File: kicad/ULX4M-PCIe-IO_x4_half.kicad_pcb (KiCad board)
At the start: 4 copper layers, 167.7 x 111.2 mm, 30 parts, among them J1 PCIexpress_bracket, J2 PCIexpress_x4, J3 SFP+, J4 SFP+, J5 Conn_02x20_Odd_Even, J6 Conn_02x05_Odd_Even, J7 Micro_SD_Card_CD, J8 Conn_02x05_Odd_Even, P2 HDMI-D, SW1 SW_DIP_x08, SW2 SW_DIP_x08, U1 Raspberry_Pi_Compute_Module_4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

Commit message: Modules update
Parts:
- removed U1: Raspberry_Pi_Compute_Module_4_Compute_Module_4_Functional, cm4:Raspberry-Pi-4-Compute-Module
- added Module1: ComputeModule4-CM4, CM4IO:Raspberry-Pi-4-Compute-Module, F.Cu at (161.2, 119.8)
- added P1: HDMI-D, hdmi-d:HDMI-D, F.Cu at (117.5, 73.9)
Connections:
- AE1 pad 1: (no net) -> unconnected-(AE1-Pad1)
- AE1 pad 2: Net-(AE1-Pad2) -> unconnected-(AE1-Pad2)
- AE2 pad 1: (no net) -> unconnected-(AE2-Pad1)
- AE2 pad 2: Net-(AE2-Pad2) -> unconnected-(AE2-Pad2)
- C1 pad 1: (no net) -> /PER0_P
- C2 pad 2: (no net) -> /PER0_N
- C3 pad 1: (no net) -> /PER1_P
- C4 pad 2: (no net) -> /PER1_N
- C5 pad 1: (no net) -> /PER2_P
- C6 pad 2: (no net) -> /PER2_N
- C7 pad 1: (no net) -> /PER3_P
- C8 pad 2: (no net) -> /PER3_N
- J2 pad A1: (no net) -> /~{PRSNT1}
- J2 pad A11: (no net) -> /~{PERST}
- J2 pad A13: (no net) -> /REFCLK+
- J2 pad A14: (no net) -> /REFCLK-
- J2 pad A19: (no net) -> unconnected-(J2-RSVD)_1
- J2 pad A32: (no net) -> unconnected-(J2-RSVD)_2
- J2 pad A5: (no net) -> /TCK
- J2 pad A6: (no net) -> /TDI
- J2 pad A7: (no net) -> /TDO
- J2 pad A8: (no net) -> /TMS
- J2 pad B10: (no net) -> +3.3VA
- J2 pad B11: (no net) -> /~{WAKE}
- J2 pad B12: (no net) -> unconnected-(J2-RSVD)_3
- J2 pad B17: (no net) -> /~{PRSNT2x1}
- J2 pad B30: (no net) -> unconnected-(J2-RSVD)
- J2 pad B31: (no net) -> /~{PRSNT2x4}
- J2 pad B5: (no net) -> /SMCLK
- J2 pad B6: (no net) -> /SMDAT
- J2 pad B9: (no net) -> /~{TRST}
- J3 pad 12: (no net) -> unconnected-(J3-RD-)
- J3 pad 13: (no net) -> unconnected-(J3-RD+)
- J3 pad 15: (no net) -> unconnected-(J3-VccR)
- J3 pad 16: (no net) -> unconnected-(J3-VccT)
- J3 pad 18: (no net) -> unconnected-(J3-TD+)
- J3 pad 19: (no net) -> unconnected-(J3-TD-)
- J3 pad 2: (no net) -> unconnected-(J3-TX_FAULT)
- J3 pad 3: (no net) -> unconnected-(J3-TX_DISABLE)
- J3 pad 4: (no net) -> unconnected-(J3-SDA)
- J3 pad 5: (no net) -> unconnected-(J3-SCL)
- J3 pad 6: (no net) -> unconnected-(J3-MOD_ABS)
- J3 pad 7: (no net) -> unconnected-(J3-RS0)
- J3 pad 8: (no net) -> unconnected-(J3-RX_LOS)
- J3 pad 9: (no net) -> unconnected-(J3-RS1)
- J3 pad CAGE: Net-(J3-PadCAGE) -> unconnected-(J3-PadCAGE)
- J4 pad 12: (no net) -> unconnected-(J4-RD-)
- J4 pad 13: (no net) -> unconnected-(J4-RD+)
- J4 pad 15: (no net) -> unconnected-(J4-VccR)
- J4 pad 16: (no net) -> unconnected-(J4-VccT)
- J4 pad 18: (no net) -> unconnected-(J4-TD+)
- J4 pad 19: (no net) -> unconnected-(J4-TD-)
- J4 pad 2: (no net) -> unconnected-(J4-TX_FAULT)
- J4 pad 3: (no net) -> unconnected-(J4-TX_DISABLE)
- J4 pad 4: (no net) -> unconnected-(J4-SDA)
- J4 pad 5: (no net) -> unconnected-(J4-SCL)
- J4 pad 6: (no net) -> unconnected-(J4-MOD_ABS)
- J4 pad 7: (no net) -> unconnected-(J4-RS0)
- J4 pad 8: (no net) -> unconnected-(J4-RX_LOS)
- J4 pad 9: (no net) -> unconnected-(J4-RS1)
- J4 pad CAGE: Net-(J4-PadCAGE) -> unconnected-(J4-PadCAGE)
- J5 pad 1: (no net) -> unconnected-(J5-Pin_1)
- J5 pad 10: (no net) -> unconnected-(J5-Pin_10)
- J5 pad 11: (no net) -> unconnected-(J5-Pin_11)
- J5 pad 12: (no net) -> unconnected-(J5-Pin_12)
- J5 pad 13: (no net) -> unconnected-(J5-Pin_13)
- J5 pad 14: (no net) -> unconnected-(J5-Pin_14)
- J5 pad 15: (no net) -> unconnected-(J5-Pin_15)
- J5 pad 16: (no net) -> unconnected-(J5-Pin_16)
- J5 pad 17: (no net) -> unconnected-(J5-Pin_17)
- J5 pad 18: (no net) -> unconnected-(J5-Pin_18)
- J5 pad 19: (no net) -> unconnected-(J5-Pin_19)
- J5 pad 2: (no net) -> unconnected-(J5-Pin_2)
- J5 pad 20: (no net) -> unconnected-(J5-Pin_20)
- J5 pad 21: (no net) -> unconnected-(J5-Pin_21)
- J5 pad 22: (no net) -> unconnected-(J5-Pin_22)
- J5 pad 23: (no net) -> unconnected-(J5-Pin_23)
- J5 pad 24: (no net) -> unconnected-(J5-Pin_24)
- J5 pad 25: (no net) -> unconnected-(J5-Pin_25)
- J5 pad 26: (no net) -> unconnected-(J5-Pin_26)
- J5 pad 27: (no net) -> unconnected-(J5-Pin_27)
- J5 pad 28: (no net) -> unconnected-(J5-Pin_28)
- J5 pad 29: (no net) -> unconnected-(J5-Pin_29)
- J5 pad 3: (no net) -> unconnected-(J5-Pin_3)
- J5 pad 30: (no net) -> unconnected-(J5-Pin_30)
- J5 pad 31: (no net) -> unconnected-(J5-Pin_31)
- J5 pad 32: (no net) -> unconnected-(J5-Pin_32)
- J5 pad 33: (no net) -> unconnected-(J5-Pin_33)
- J5 pad 34: (no net) -> unconnected-(J5-Pin_34)
- J5 pad 35: (no net) -> unconnected-(J5-Pin_35)
- J5 pad 36: (no net) -> unconnected-(J5-Pin_36)
- J5 pad 37: (no net) -> unconnected-(J5-Pin_37)
- J5 pad 38: (no net) -> unconnected-(J5-Pin_38)
- J5 pad 39: (no net) -> unconnected-(J5-Pin_39)
- J5 pad 4: (no net) -> unconnected-(J5-Pin_4)
- J5 pad 40: (no net) -> unconnected-(J5-Pin_40)
- J5 pad 5: (no net) -> unconnected-(J5-Pin_5)
- J5 pad 6: (no net) -> unconnected-(J5-Pin_6)
- J5 pad 7: (no net) -> unconnected-(J5-Pin_7)
- J5 pad 8: (no net) -> unconnected-(J5-Pin_8)
- J5 pad 9: (no net) -> unconnected-(J5-Pin_9)
- J6 pad 1: (no net) -> unconnected-(J6-Pin_1)
- J6 pad 10: (no net) -> unconnected-(J6-Pin_10)
- J6 pad 2: (no net) -> unconnected-(J6-Pin_2)
- J6 pad 3: (no net) -> unconnected-(J6-Pin_3)
- J6 pad 4: (no net) -> unconnected-(J6-Pin_4)
- J6 pad 5: (no net) -> unconnected-(J6-Pin_5)
- J6 pad 6: (no net) -> unconnected-(J6-Pin_6)
- J6 pad 7: (no net) -> unconnected-(J6-Pin_7)
- J6 pad 8: (no net) -> unconnected-(J6-Pin_8)
- J6 pad 9: (no net) -> unconnected-(J6-Pin_9)
- J7 pad 1: (no net) -> unconnected-(J7-DAT2)
- J7 pad 10: (no net) -> unconnected-(J7-CD)_1
- J7 pad 11: (no net) -> unconnected-(J7-CD)
- J7 pad 2: (no net) -> unconnected-(J7-DAT3/CD)
- J7 pad 3: (no net) -> unconnected-(J7-CMD)
- J7 pad 4: (no net) -> unconnected-(J7-VDD)
- J7 pad 5: (no net) -> unconnected-(J7-CLK)
- J7 pad 6: (no net) -> unconnected-(J7-VSS)
- J7 pad 7: (no net) -> unconnected-(J7-DAT0)
- J7 pad 8: (no net) -> unconnected-(J7-DAT1)
- J7 pad 9: Net-(J7-Pad9) -> unconnected-(J7-SHIELD)
- J8 pad 1: (no net) -> unconnected-(J8-Pin_1)
- J8 pad 10: (no net) -> unconnected-(J8-Pin_10)
- J8 pad 2: (no net) -> unconnected-(J8-Pin_2)
- J8 pad 3: (no net) -> unconnected-(J8-Pin_3)
- J8 pad 4: (no net) -> unconnected-(J8-Pin_4)
- J8 pad 5: (no net) -> unconnected-(J8-Pin_5)
- J8 pad 6: (no net) -> unconnected-(J8-Pin_6)
- J8 pad 7: (no net) -> unconnected-(J8-Pin_7)
- J8 pad 8: (no net) -> unconnected-(J8-Pin_8)
- J8 pad 9: (no net) -> unconnected-(J8-Pin_9)
- P2 pad 0: Net-(P2-Pad0) -> unconnected-(P2-Pad0)
- P2 pad 1: (no net) -> unconnected-(P2-P1)
- P2 pad 10: (no net) -> unconnected-(P2-P10)
- P2 pad 11: (no net) -> unconnected-(P2-P11)
- P2 pad 12: (no net) -> unconnected-(P2-P12)
- P2 pad 13: (no net) -> unconnected-(P2-P13)
- P2 pad 14: (no net) -> unconnected-(P2-P14)
- P2 pad 15: (no net) -> unconnected-(P2-P15)
- P2 pad 16: (no net) -> unconnected-(P2-P16)
- P2 pad 17: (no net) -> unconnected-(P2-P17)
- P2 pad 18: (no net) -> unconnected-(P2-P18)
- P2 pad 19: (no net) -> unconnected-(P2-P19)
- P2 pad 2: (no net) -> unconnected-(P2-P2)
- P2 pad 3: (no net) -> unconnected-(P2-P3)
- P2 pad 4: (no net) -> unconnected-(P2-P4)
- P2 pad 5: (no net) -> unconnected-(P2-P5)
- P2 pad 6: (no net) -> unconnected-(P2-P6)
- P2 pad 7: (no net) -> unconnected-(P2-P7)
- P2 pad 8: (no net) -> unconnected-(P2-P8)
- P2 pad 9: (no net) -> unconnected-(P2-P9)
- SW1 pad 1: (no net) -> unconnected-(SW1-Pad1)
- SW1 pad 10: (no net) -> unconnected-(SW1-Pad10)
- SW1 pad 11: (no net) -> unconnected-(SW1-Pad11)
- SW1 pad 12: (no net) -> unconnected-(SW1-Pad12)
- SW1 pad 13: (no net) -> unconnected-(SW1-Pad13)
- SW1 pad 14: (no net) -> unconnected-(SW1-Pad14)
- SW1 pad 15: (no net) -> unconnected-(SW1-Pad15)
- SW1 pad 16: (no net) -> unconnected-(SW1-Pad16)
- SW1 pad 2: (no net) -> unconnected-(SW1-Pad2)
- SW1 pad 3: (no net) -> unconnected-(SW1-Pad3)
- SW1 pad 4: (no net) -> unconnected-(SW1-Pad4)
- SW1 pad 5: (no net) -> unconnected-(SW1-Pad5)
- SW1 pad 6: (no net) -> unconnected-(SW1-Pad6)
- SW1 pad 7: (no net) -> unconnected-(SW1-Pad7)
- SW1 pad 8: (no net) -> unconnected-(SW1-Pad8)
- SW1 pad 9: (no net) -> unconnected-(SW1-Pad9)
- SW2 pad 1: (no net) -> unconnected-(SW2-Pad1)
- SW2 pad 10: (no net) -> unconnected-(SW2-Pad10)
- SW2 pad 11: (no net) -> unconnected-(SW2-Pad11)
- SW2 pad 12: (no net) -> unconnected-(SW2-Pad12)
- SW2 pad 13: (no net) -> unconnected-(SW2-Pad13)
- SW2 pad 14: (no net) -> unconnected-(SW2-Pad14)
- SW2 pad 15: (no net) -> unconnected-(SW2-Pad15)
- SW2 pad 16: (no net) -> unconnected-(SW2-Pad16)
- SW2 pad 2: (no net) -> unconnected-(SW2-Pad2)
- SW2 pad 3: (no net) -> unconnected-(SW2-Pad3)
- SW2 pad 4: (no net) -> unconnected-(SW2-Pad4)
- SW2 pad 5: (no net) -> unconnected-(SW2-Pad5)
- SW2 pad 6: (no net) -> unconnected-(SW2-Pad6)
- SW2 pad 7: (no net) -> unconnected-(SW2-Pad7)
- SW2 pad 8: (no net) -> unconnected-(SW2-Pad8)
- SW2 pad 9: (no net) -> unconnected-(SW2-Pad9)

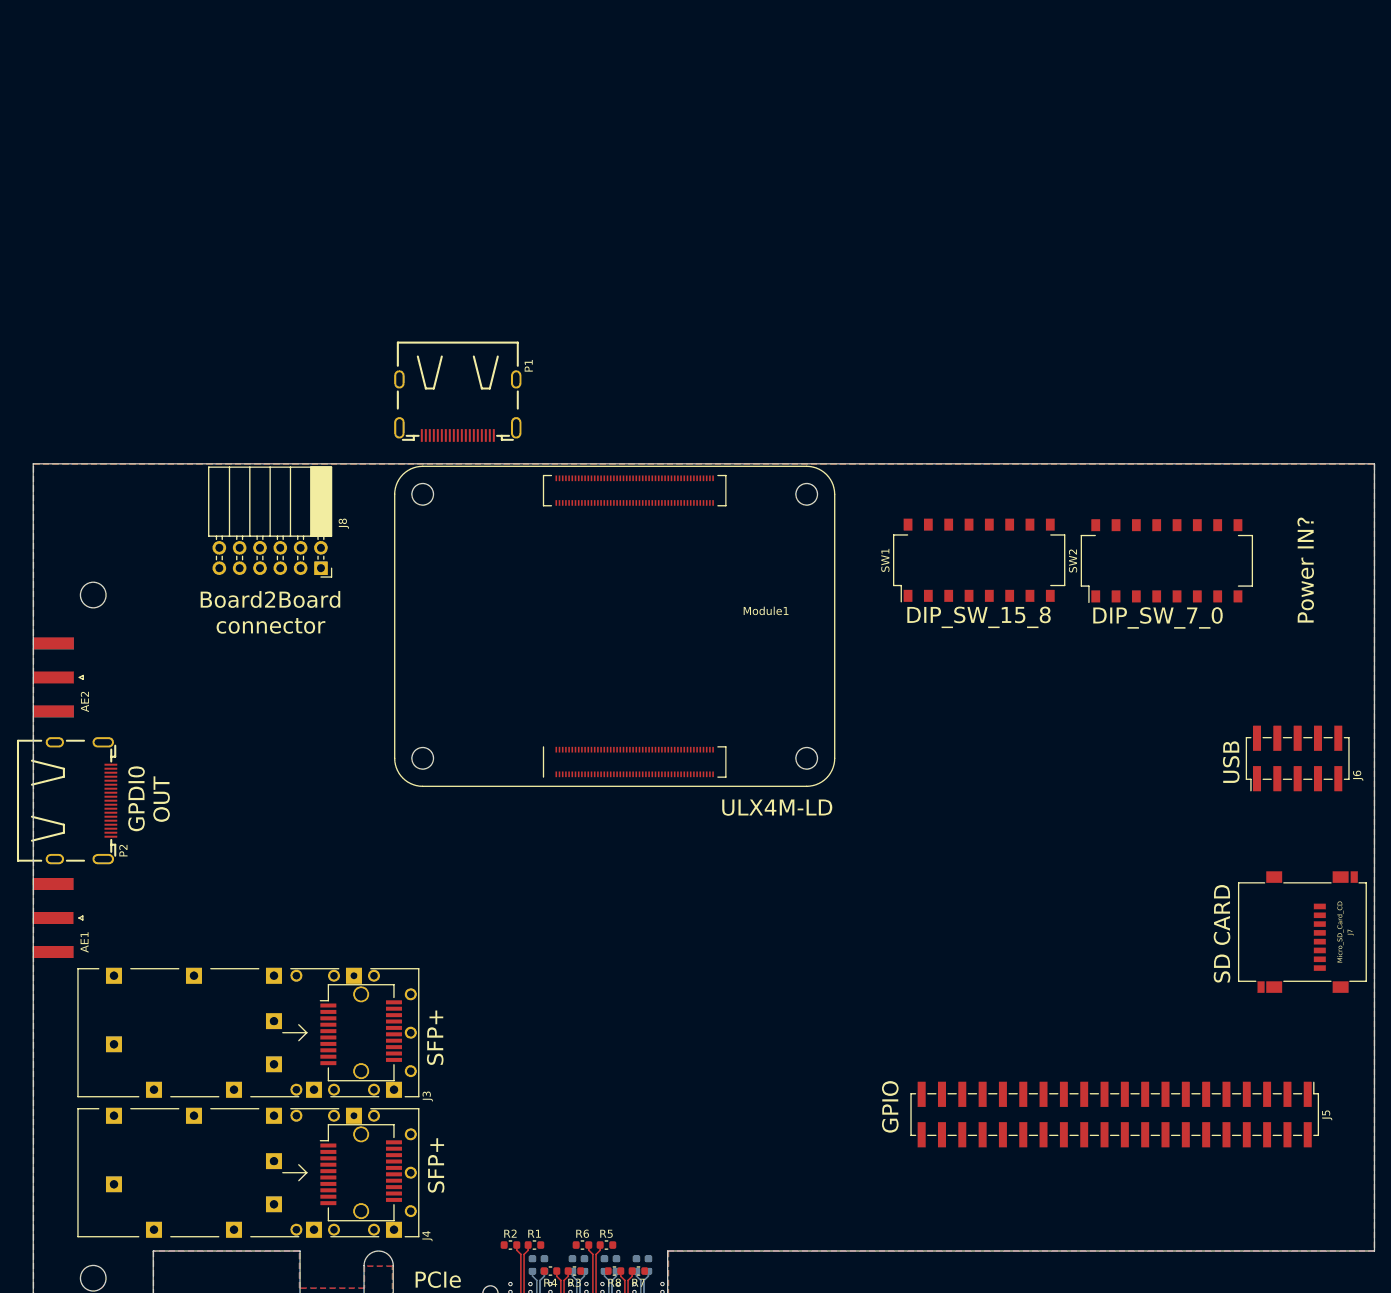
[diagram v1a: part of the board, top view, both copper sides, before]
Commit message: Adding SPDIF
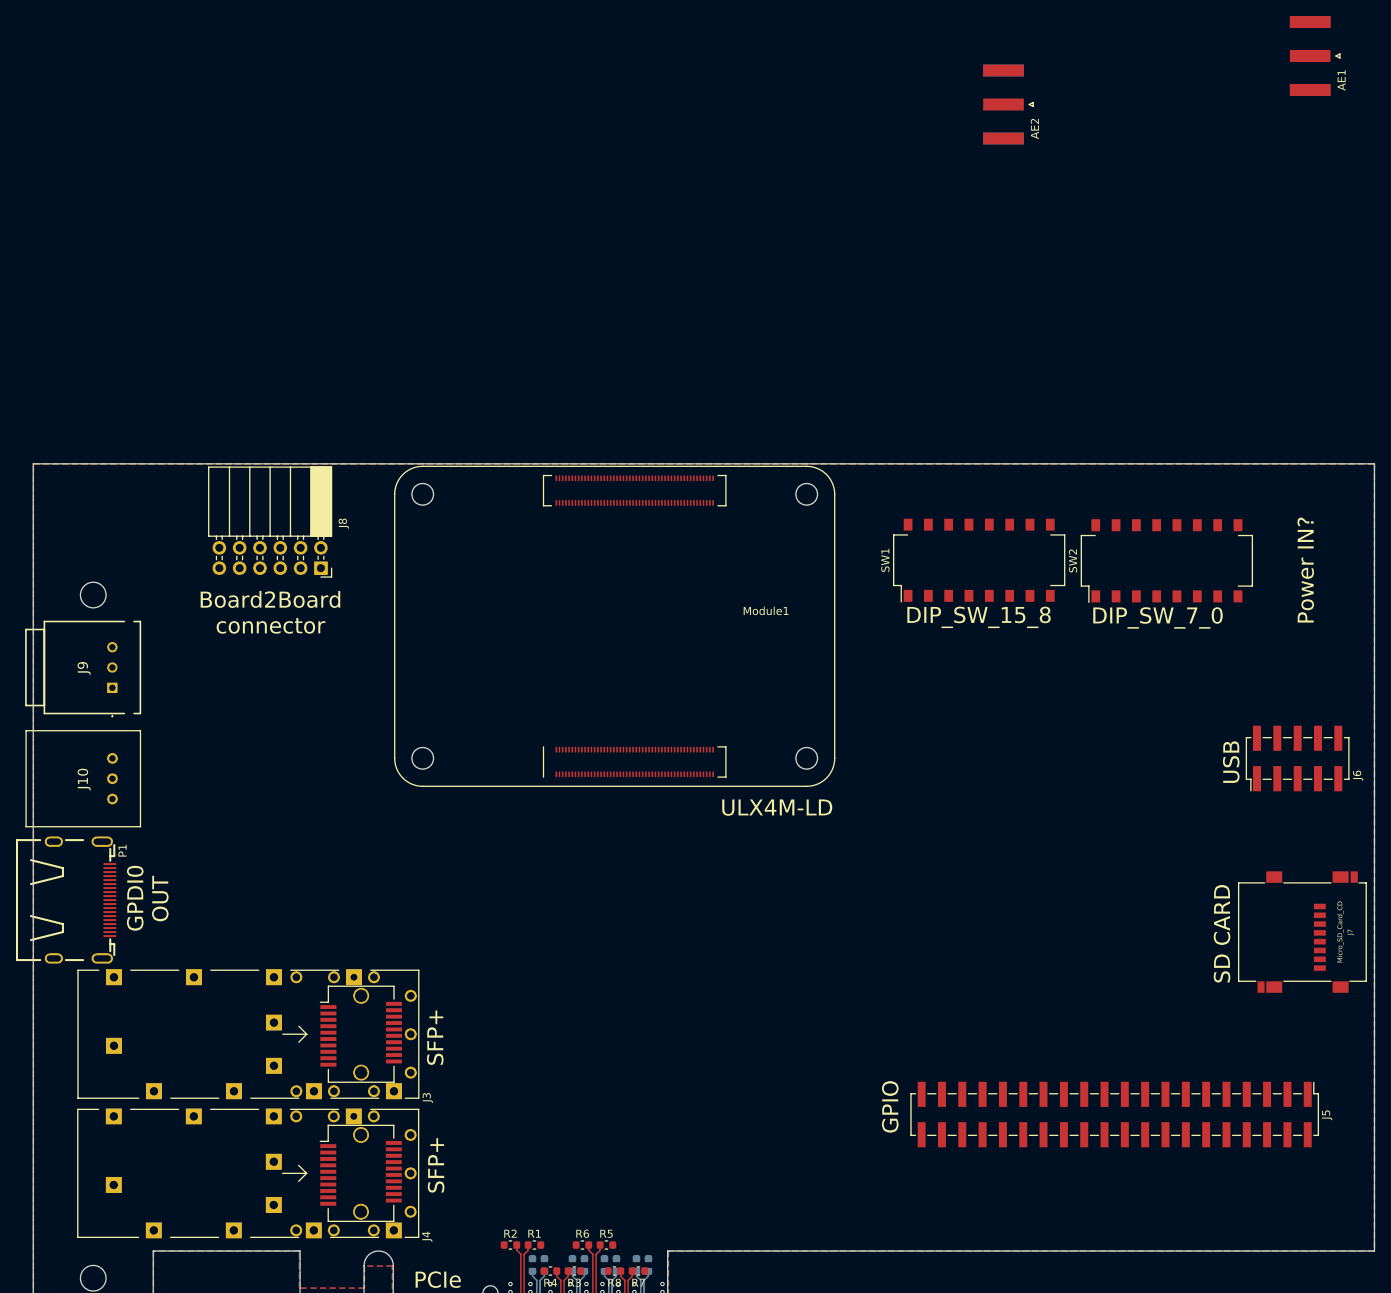
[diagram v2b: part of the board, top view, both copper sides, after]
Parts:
- removed P2: HDMI-D, hdmi-d:HDMI-D
- added J10: FCR684205R, FCR684205-R:FCR684205R, F.Cu at (74.4, 119.8)
- added J9: FCR684205T, FCR684205-T:FCR684205T, F.Cu at (74.4, 111.0)
- moved AE1 190.5 mm to (224.1, 32.0)
- moved AE2 138.7 mm to (185.8, 38.1)
- moved P1 80.3 mm to (68.5, 137.5), turned to 180 degrees
- moved J3 0.19 mm to (111.7, 154.3)
- moved J4 0.08 mm to (111.6, 171.7)
